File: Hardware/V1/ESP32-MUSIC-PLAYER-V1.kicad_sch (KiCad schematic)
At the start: 70 parts, among them J1 DC-IN, J10 HDR4, J11 EXP1, J2 JST PH4, J3 JST XH4, J4 SHOU-HAN-TF-PUSH, J7 Keystone 900, J8 Keystone 900, J9 Conn_01x02, M1 CN3903 5V/3A Module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

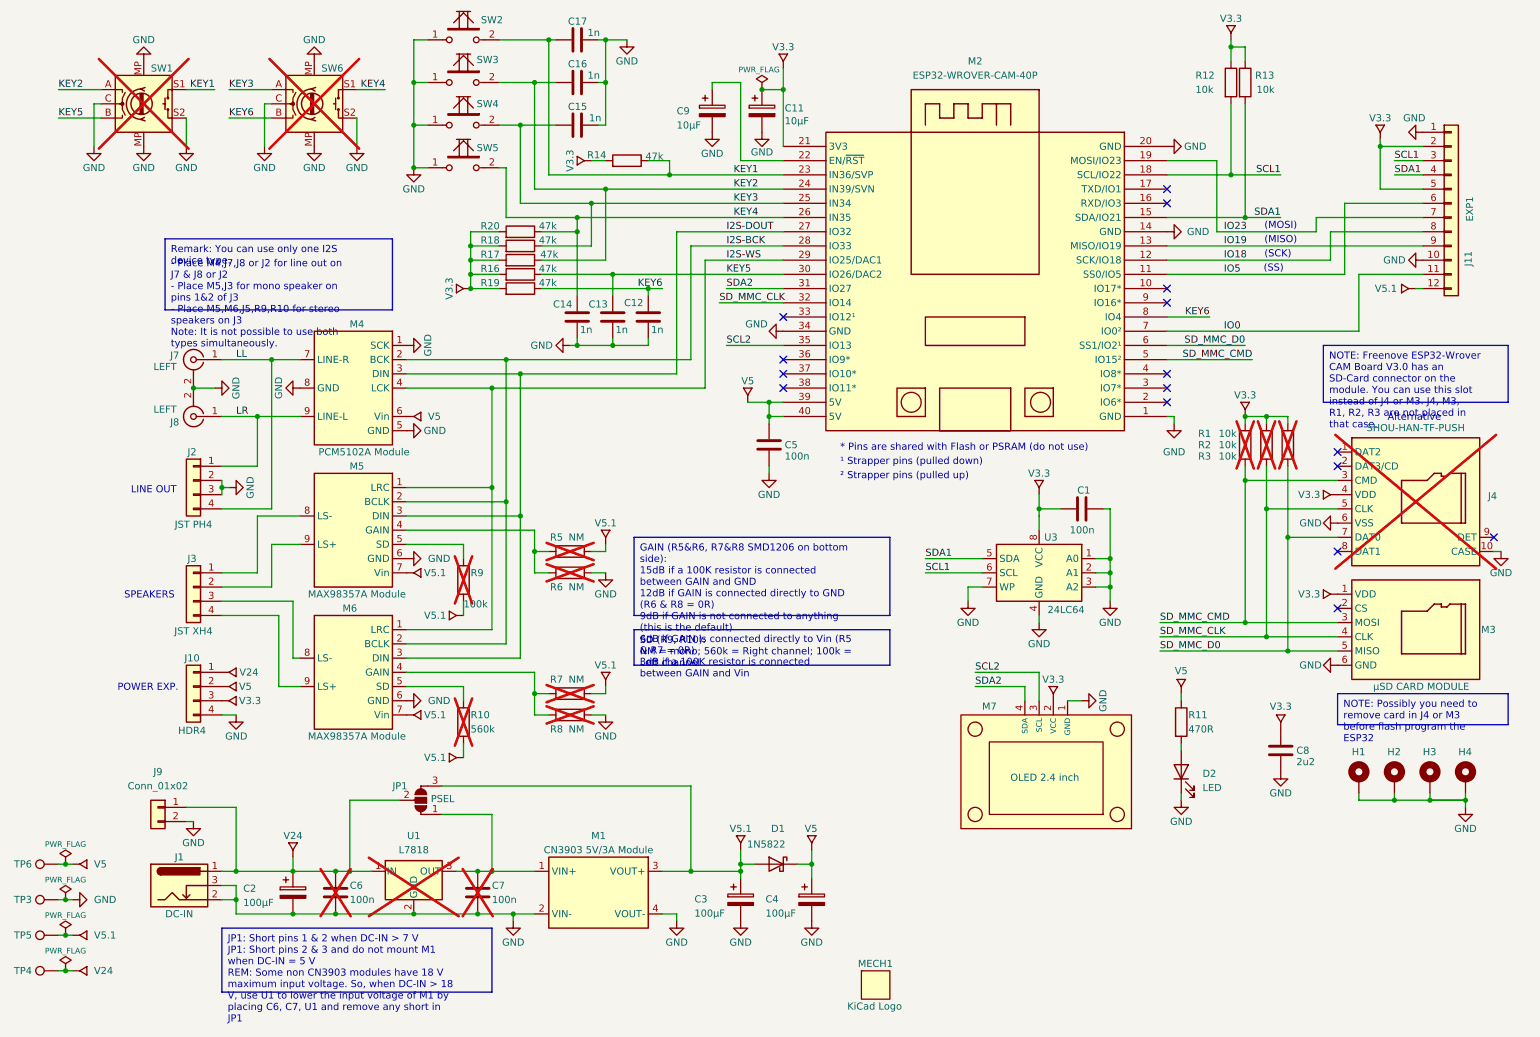
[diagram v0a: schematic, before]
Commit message: Renamed V24 to Vin
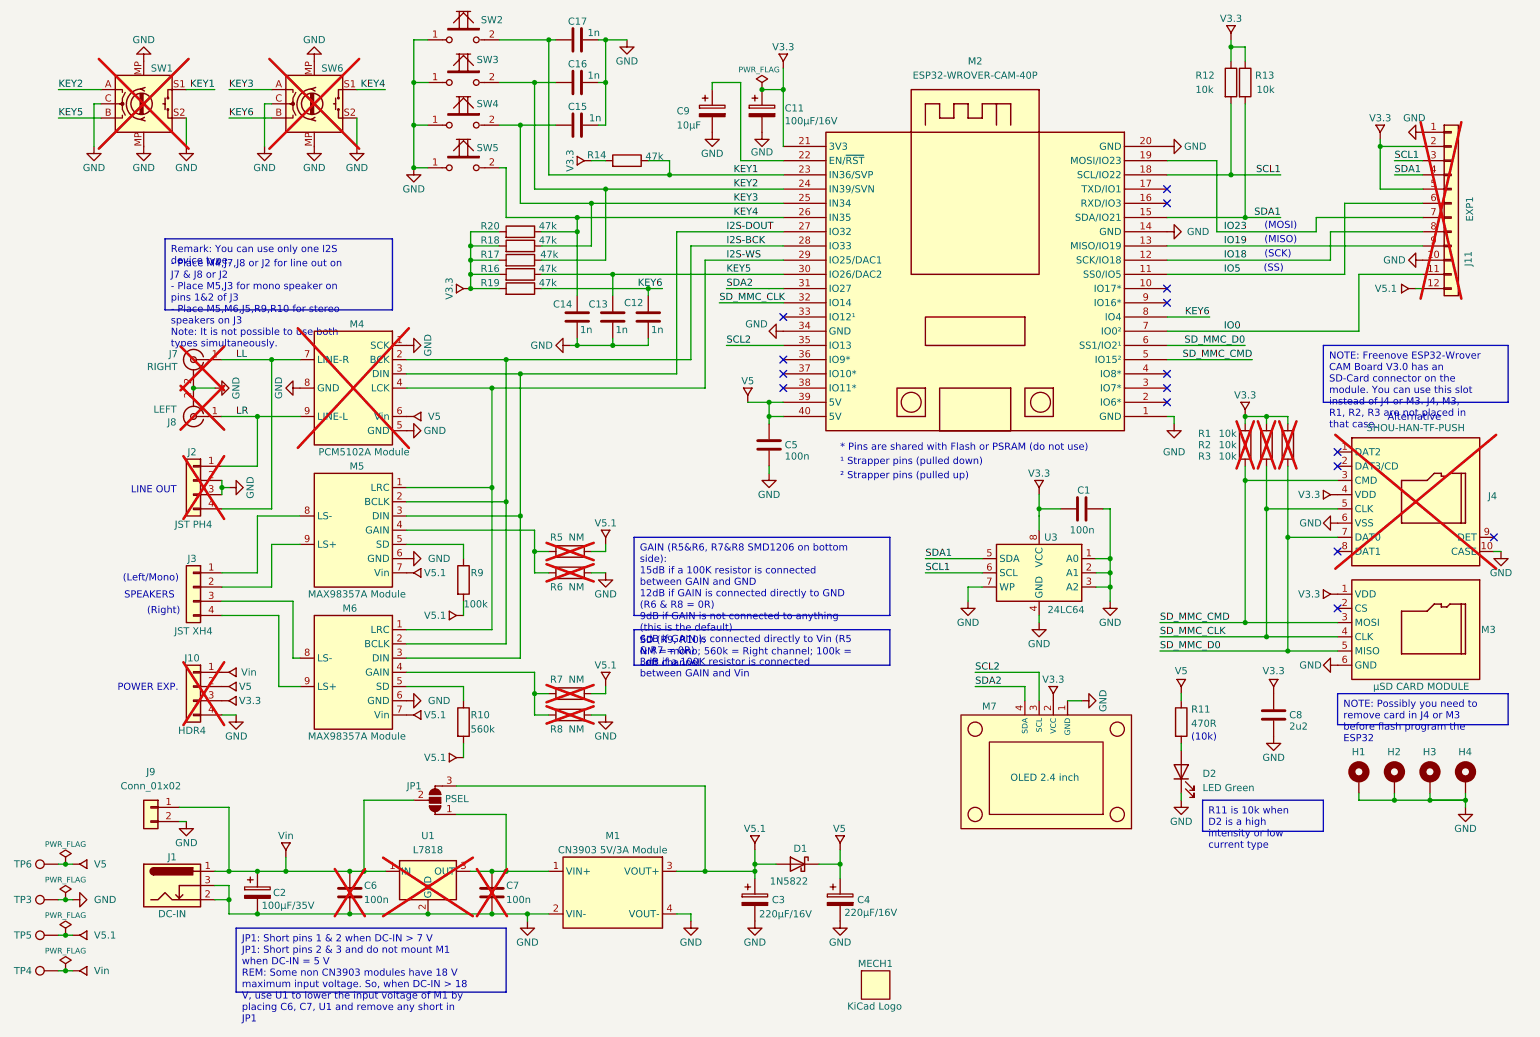
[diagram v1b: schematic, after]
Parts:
- C11: value 10µF -> 100µF/16V
- C2: value 100µF -> 100µF/35V
- C3, C4: value 100µF -> 220µF/16V
- D2: value LED -> LED Green
- J10, J11, J2, J8, M4: now not fitted
- J7: Comment LEFT -> RIGHT; now not fitted
- R10, R9: now fitted
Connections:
- net V24 renamed Vin
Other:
- note added: "(10k)"
- note added: "(Left/Mono)"
- note added: "(Right)"
- moved on the sheet: C2, C3, C4, C6, C7, C8, D1, J1, J9, JP1, M1, U1

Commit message: Add files via upload
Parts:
- JP1: symbol !Gloeidraad:SolderJumper_3_B_ -> !Gloeidraad:Jumper_3_type_2; now left out of the parts list
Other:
- moved on the sheet: C3, C4, D1
